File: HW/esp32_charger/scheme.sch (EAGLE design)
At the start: 23 parts, among them IC3 24C01SN, K1 4052, T1 2N7002E, T2 2N7002E

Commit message: Updated project and gitignore
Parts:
- added C2: 10uF, rcl:C-EUC0805
- added C2-TANT: 22uF, rcl:C-EUC3216
- added IC1: LM1117IMPX-3.3, lm1117:LM1117IMPX-3.3
- added LED1: (no value), led:LEDCHIP-LED0805
- added R9: 500, rcl:R-EU_R0805
- added SV2: (no value), con-lstb:MA03-1
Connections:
- new net +3V3: C2-TANT.1, IC1.OUT, IC1.OUT1, U$1.3V3
- new net +5V: C2.1, IC1.IN, R9.2, SV2.2
- new net N$1: LED1.A, R9.1
- net GND: now also C2-TANT.2, C2.2, IC1.GND, LED1.C, SV2.1
- net VCC: no longer U$1.3V3
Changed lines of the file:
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@@
 <?xml version="1.0" encoding="utf-8"?>
 <!DOCTYPE eagle SYSTEM "eagle.dtd">
-<eagle version="9.3.2">
+<eagle version="9.4.2">
 <drawing>
 <settings>
@@
 <setting verticaltext="up"/>
 </settings>
-<grid distance="0.1" unitdist="inch" unit="inch" style="dots" multiple="1" display="yes" altdistance="0.01" altunitdist="inch" altunit="inch"/>
+<grid distance="0.1" unitdist="inch" unit="inch" style="lines" multiple="1" display="no" altdistance="0.01" altunitdist="inch" altunit="inch"/>
 <layers>
 <layer number="1" name="Top" color="4" fill="1" visible="no" active="no"/>
@@
 <layer number="230" name="230bmp" color="7" fill="1" visible="yes" active="yes"/>
 <layer number="231" name="231bmp" color="7" fill="1" visible="yes" active="yes"/>
+<layer number="232" name="Eagle3D_PG2" color="7" fill="1" visible="no" active="no"/>
+<layer number="233" name="Eagle3D_PG3" color="7" fill="1" visible="no" active="no"/>
 <layer number="248" name="Housing" color="7" fill="1" visible="yes" active="yes"/>
 <layer number="249" name="Edge" color="7" fill="1" visible="yes" active="yes"/>
@@
 <part name="K1" library="relay" library_urn="urn:adsk.eagle:library:339" deviceset="4052" device="" package3d_urn="urn:adsk.eagle:package:24305/1"/>
 <part name="T1" library="nxp_60" deviceset="2N7002" device="" technology="E"/>
-<part name="SUPPLY1" library="SparkFun-PowerSymbols" library_urn="urn:adsk.eagle:library:530" deviceset="VCC" device=""/>
 <part name="GND1" library="SparkFun-PowerSymbols" library_urn="urn:adsk.eagle:library:530" deviceset="GND" device=""/>
 <part name="SUPPLY2" library="SparkFun-PowerSymbols" library_urn="urn:adsk.eagle:library:530" deviceset="VCC" device=""/>
@@
 <part name="R8" library="antduino" deviceset="SPARKFUN_RESISTOR" device="PTH-1/2W" value="10K"/>
 <part name="SUPPLY4" library="SparkFun-PowerSymbols" library_urn="urn:adsk.eagle:library:530" deviceset="VCC" device=""/>
+<part name="IC1" library="lm1117" deviceset="LM1117IMPX-*" device="" technology="3.3"/>
+<part name="GND8" library="supply1" library_urn="urn:adsk.eagle:library:371" deviceset="GND" device=""/>
+<part name="P+1" library="supply1" library_urn="urn:adsk.eagle:library:371" deviceset="+5V" device=""/>
+<part name="SV2" library="con-lstb" library_urn="urn:adsk.eagle:library:162" deviceset="MA03-1" device="" package3d_urn="urn:adsk.eagle:package:8339/1"/>
+<part name="+3V1" library="supply1" library_urn="urn:adsk.eagle:library:371" deviceset="+3V3" device=""/>
+<part name="+3V2" library="supply1" library_urn="urn:adsk.eagle:library:371" deviceset="+3V3" device=""/>
+<part name="C2" library="rcl" library_urn="urn:adsk.eagle:library:334" deviceset="C-EU" device="C0805" package3d_urn="urn:adsk.eagle:package:23617/2" value="10uF"/>
+<part name="C2-TANT" library="rcl" library_urn="urn:adsk.eagle:library:334" deviceset="C-EU" device="C3216" package3d_urn="urn:adsk.eagle:package:23628/2" value="22uF"/>
+<part name="R9" library="rcl" library_urn="urn:adsk.eagle:library:334" deviceset="R-EU_" device="R0805" package3d_urn="urn:adsk.eagle:package:23553/2" value="500"/>
+<part name="LED1" library="led" library_urn="urn:adsk.eagle:library:259" deviceset="LED" device="CHIP-LED0805" package3d_urn="urn:adsk.eagle:package:15818/2"/>
 </parts>
 <sheets>
@@
 <attribute name="NAME" x="-2.54" y="90.17" size="1.778" layer="95" font="vector" rot="R180"/>
 </instance>
-<instance part="SUPPLY1" gate="G$1" x="55.88" y="45.72" smashed="yes" rot="R180">
-<attribute name="VALUE" x="55.88" y="42.926" size="1.778" layer="96" rot="R270" align="bottom-center"/>
-</instance>
 <instance part="GND1" gate="1" x="60.96" y="38.1" smashed="yes">
 <attribute name="VALUE" x="60.96" y="37.846" size="1.778" layer="96" align="top-center"/>
@@
 <instance part="SUPPLY4" gate="G$1" x="114.3" y="0" smashed="yes">
 <attribute name="VALUE" x="114.3" y="2.794" size="1.778" layer="96" rot="R90" align="bottom-center"/>
+</instance>
+<instance part="IC1" gate="G$1" x="30.48" y="2.54" smashed="yes">
+<attribute name="NAME" x="33.02" y="-5.08" size="1.778" layer="95"/>
+<attribute name="VALUE" x="20.32" y="10.16" size="1.778" layer="96"/>
+</instance>
+<instance part="GND8" gate="1" x="30.48" y="-30.48" smashed="yes">
+<attribute name="VALUE" x="27.94" y="-33.02" size="1.778" layer="96"/>
+</instance>
+<instance part="P+1" gate="1" x="-5.08" y="5.08" smashed="yes">
+<attribute name="VALUE" x="-7.62" y="0" size="1.778" layer="96" rot="R90"/>
+</instance>
+<instance part="SV2" gate="G$1" x="-5.08" y="-33.02" smashed="yes" rot="R90">
+<attribute name="VALUE" x="2.54" y="-34.29" size="1.778" layer="96" rot="R90"/>
+<attribute name="NAME" x="-10.922" y="-34.29" size="1.778" layer="95" rot="R90"/>
+</instance>
+<instance part="+3V1" gate="G$1" x="66.04" y="55.88" smashed="yes">
+<attribute name="VALUE" x="63.5" y="50.8" size="1.778" layer="96" rot="R90"/>
+</instance>
+<instance part="+3V2" gate="G$1" x="58.42" y="10.16" smashed="yes">
+<attribute name="VALUE" x="55.88" y="5.08" size="1.778" layer="96" rot="R90"/>
+</instance>
+<instance part="C2" gate="G$1" x="15.24" y="0" smashed="yes">
+<attribute name="NAME" x="16.764" y="0.381" size="1.778" layer="95"/>
+<attribute name="VALUE" x="16.764" y="-4.699" size="1.778" layer="96"/>
+</instance>
+<instance part="C2-TANT" gate="G$1" x="45.72" y="2.54" smashed="yes">
+<attribute name="NAME" x="47.244" y="2.921" size="1.778" layer="95"/>
+<attribute name="VALUE" x="47.244" y="-2.159" size="1.778" layer="96"/>
+</instance>
+<instance part="R9" gate="G$1" x="2.54" y="-2.54" smashed="yes" rot="R90">
+<attribute name="NAME" x="1.0414" y="-6.35" size="1.778" layer="95" rot="R90"/>
+<attribute name="VALUE" x="5.842" y="-6.35" size="1.778" layer="96" rot="R90"/>
+</instance>
+<instance part="LED1" gate="G$1" x="2.54" y="-12.7" smashed="yes">
+<attribute name="NAME" x="6.096" y="-17.272" size="1.778" layer="95" rot="R90"/>
+<attribute name="VALUE" x="8.255" y="-17.272" size="1.778" layer="96" rot="R90"/>
 </instance>
 </instances>
@@
 <nets>
 <net name="VCC" class="0">
-<segment>
-<pinref part="U$1" gate="G$1" pin="3V3"/>
-<pinref part="SUPPLY1" gate="G$1" pin="VCC"/>
-<wire x1="55.88" y1="48.26" x2="55.88" y2="45.72" width="0.1524" layer="91"/>
-</segment>
 <segment>
 <pinref part="U$3" gate="G$1" pin="VCC"/>
@@
 <wire x1="114.3" y1="-29.464" x2="114.3" y2="-27.94" width="0.1524" layer="91"/>
 <junction x="114.3" y="-27.94"/>
+</segment>
+<segment>
+<pinref part="IC1" gate="G$1" pin="GND"/>
+<pinref part="SV2" gate="G$1" pin="1"/>
+<wire x1="-2.54" y1="-25.4" x2="2.54" y2="-25.4" width="0.1524" layer="91"/>
+<wire x1="2.54" y1="-25.4" x2="30.48" y2="-25.4" width="0.1524" layer="91"/>
+<wire x1="30.48" y1="-25.4" x2="30.48" y2="-5.08" width="0.1524" layer="91"/>
+<pinref part="GND8" gate="1" pin="GND"/>
+<wire x1="30.48" y1="-27.94" x2="30.48" y2="-25.4" width="0.1524" layer="91"/>
+<junction x="30.48" y="-25.4"/>
+<pinref part="LED1" gate="G$1" pin="C"/>
+<wire x1="2.54" y1="-17.78" x2="2.54" y2="-25.4" width="0.1524" layer="91"/>
+<junction x="2.54" y="-25.4"/>
+<pinref part="C2" gate="G$1" pin="2"/>
+<wire x1="15.24" y1="-5.08" x2="30.48" y2="-5.08" width="0.1524" layer="91"/>
+<junction x="30.48" y="-5.08"/>
+<pinref part="C2-TANT" gate="G$1" pin="2"/>
+<wire x1="45.72" y1="-2.54" x2="45.72" y2="-5.08" width="0.1524" layer="91"/>
+<wire x1="45.72" y1="-5.08" x2="30.48" y2="-5.08" width="0.1524" layer="91"/>
 </segment>
 </net>
@@
 </segment>
 </net>
+<net name="+5V" class="0">
+<segment>
+<pinref part="P+1" gate="1" pin="+5V"/>
+<pinref part="IC1" gate="G$1" pin="IN"/>
+<wire x1="-5.08" y1="2.54" x2="2.54" y2="2.54" width="0.1524" layer="91"/>
+<pinref part="SV2" gate="G$1" pin="2"/>
+<wire x1="2.54" y1="2.54" x2="15.24" y2="2.54" width="0.1524" layer="91"/>
+<wire x1="15.24" y1="2.54" x2="22.86" y2="2.54" width="0.1524" layer="91"/>
+<wire x1="-5.08" y1="-25.4" x2="-5.08" y2="2.54" width="0.1524" layer="91"/>
+<junction x="-5.08" y="2.54"/>
+<pinref part="R9" gate="G$1" pin="2"/>
+<junction x="2.54" y="2.54"/>
+<pinref part="C2" gate="G$1" pin="1"/>
+<junction x="15.24" y="2.54"/>
+</segment>
+</net>
+<net name="+3V3" class="0">
+<segment>
+<pinref part="IC1" gate="G$1" pin="OUT"/>
+<pinref part="IC1" gate="G$1" pin="OUT1"/>
+<wire x1="38.1" y1="2.54" x2="38.1" y2="5.08" width="0.1524" layer="91"/>
+<pinref part="+3V2" gate="G$1" pin="+3V3"/>
+<wire x1="38.1" y1="5.08" x2="45.72" y2="5.08" width="0.1524" layer="91"/>
+<wire x1="45.72" y1="5.08" x2="58.42" y2="5.08" width="0.1524" layer="91"/>
+<wire x1="58.42" y1="5.08" x2="58.42" y2="7.62" width="0.1524" layer="91"/>
+<junction x="38.1" y="5.08"/>
+<pinref part="C2-TANT" gate="G$1" pin="1"/>
+<junction x="45.72" y="5.08"/>
+</segment>
+<segment>
+<pinref part="U$1" gate="G$1" pin="3V3"/>
+<wire x1="55.88" y1="48.26" x2="66.04" y2="48.26" width="0.1524" layer="91"/>
+<pinref part="+3V1" gate="G$1" pin="+3V3"/>
+<wire x1="66.04" y1="48.26" x2="66.04" y2="53.34" width="0.1524" layer="91"/>
+</segment>
+</net>
+<net name="N$1" class="0">
+<segment>
+<pinref part="R9" gate="G$1" pin="1"/>
+<pinref part="LED1" gate="G$1" pin="A"/>
+<wire x1="2.54" y1="-10.16" x2="2.54" y2="-7.62" width="0.1524" layer="91"/>
+</segment>
+</net>

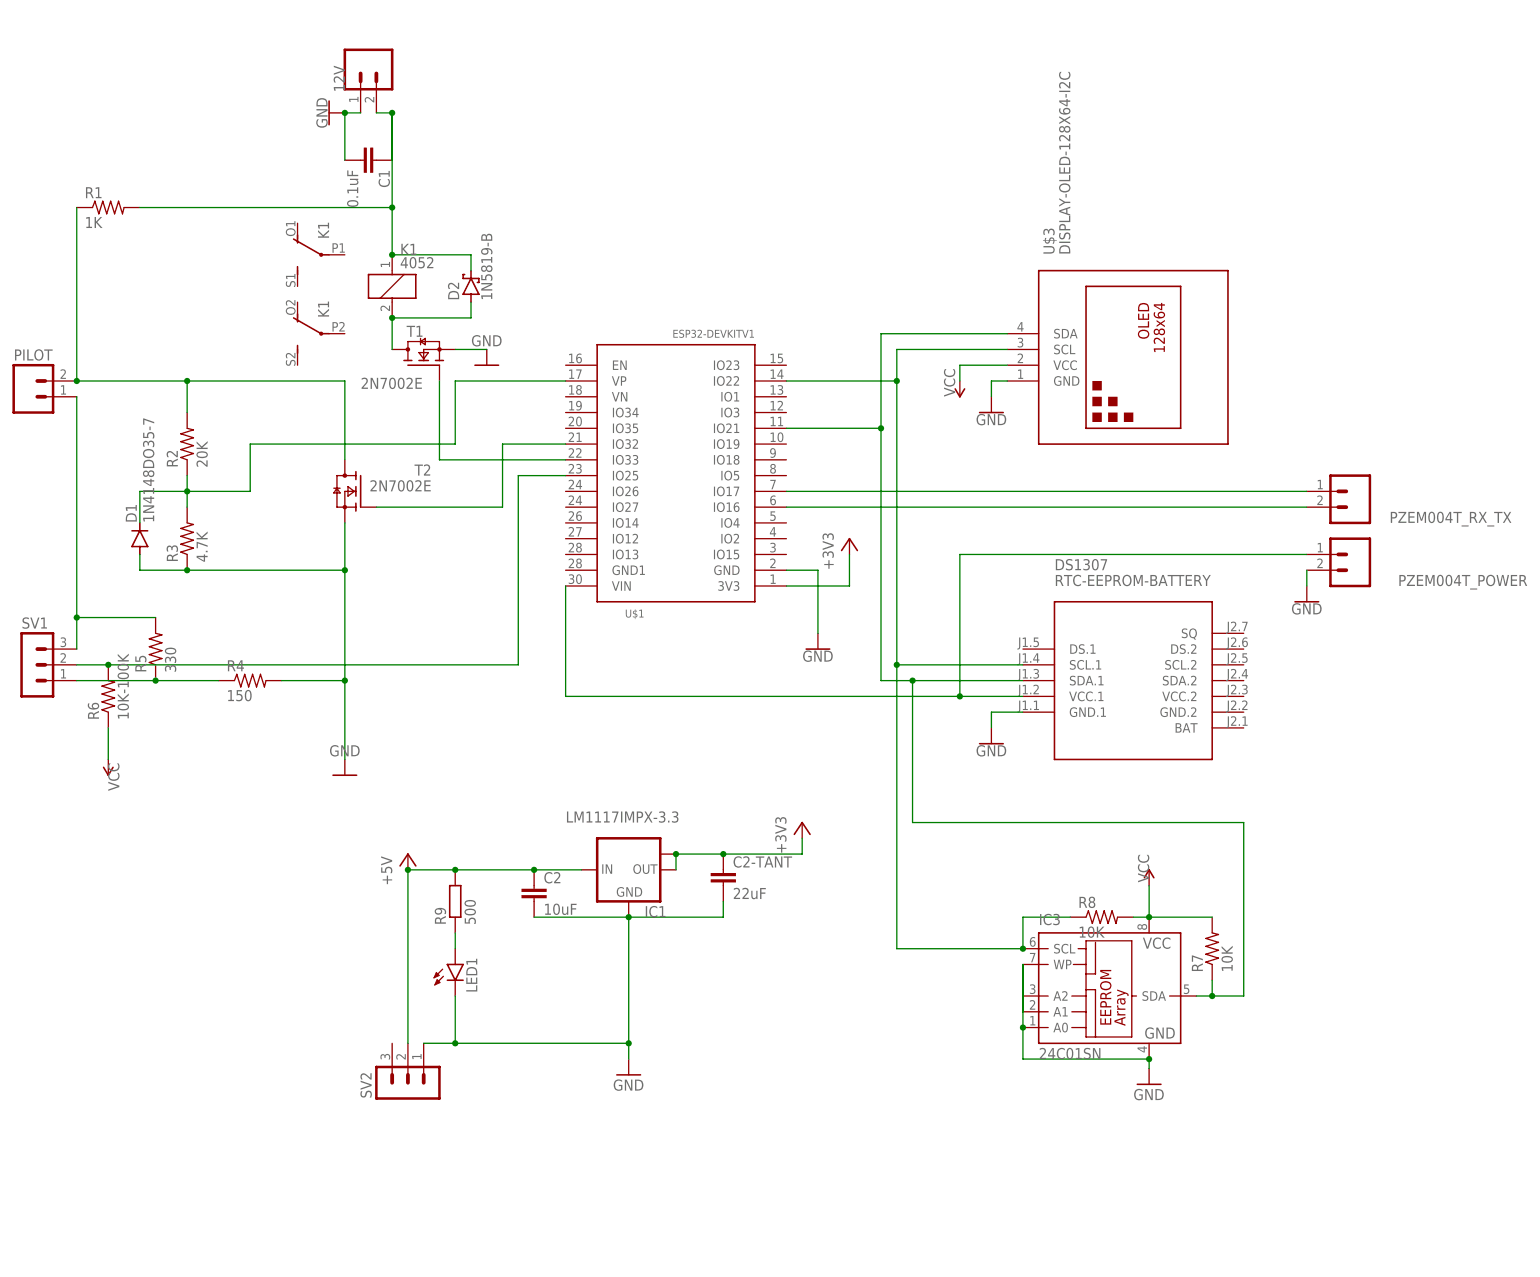
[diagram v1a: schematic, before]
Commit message: Added bare esp32 and ds1307
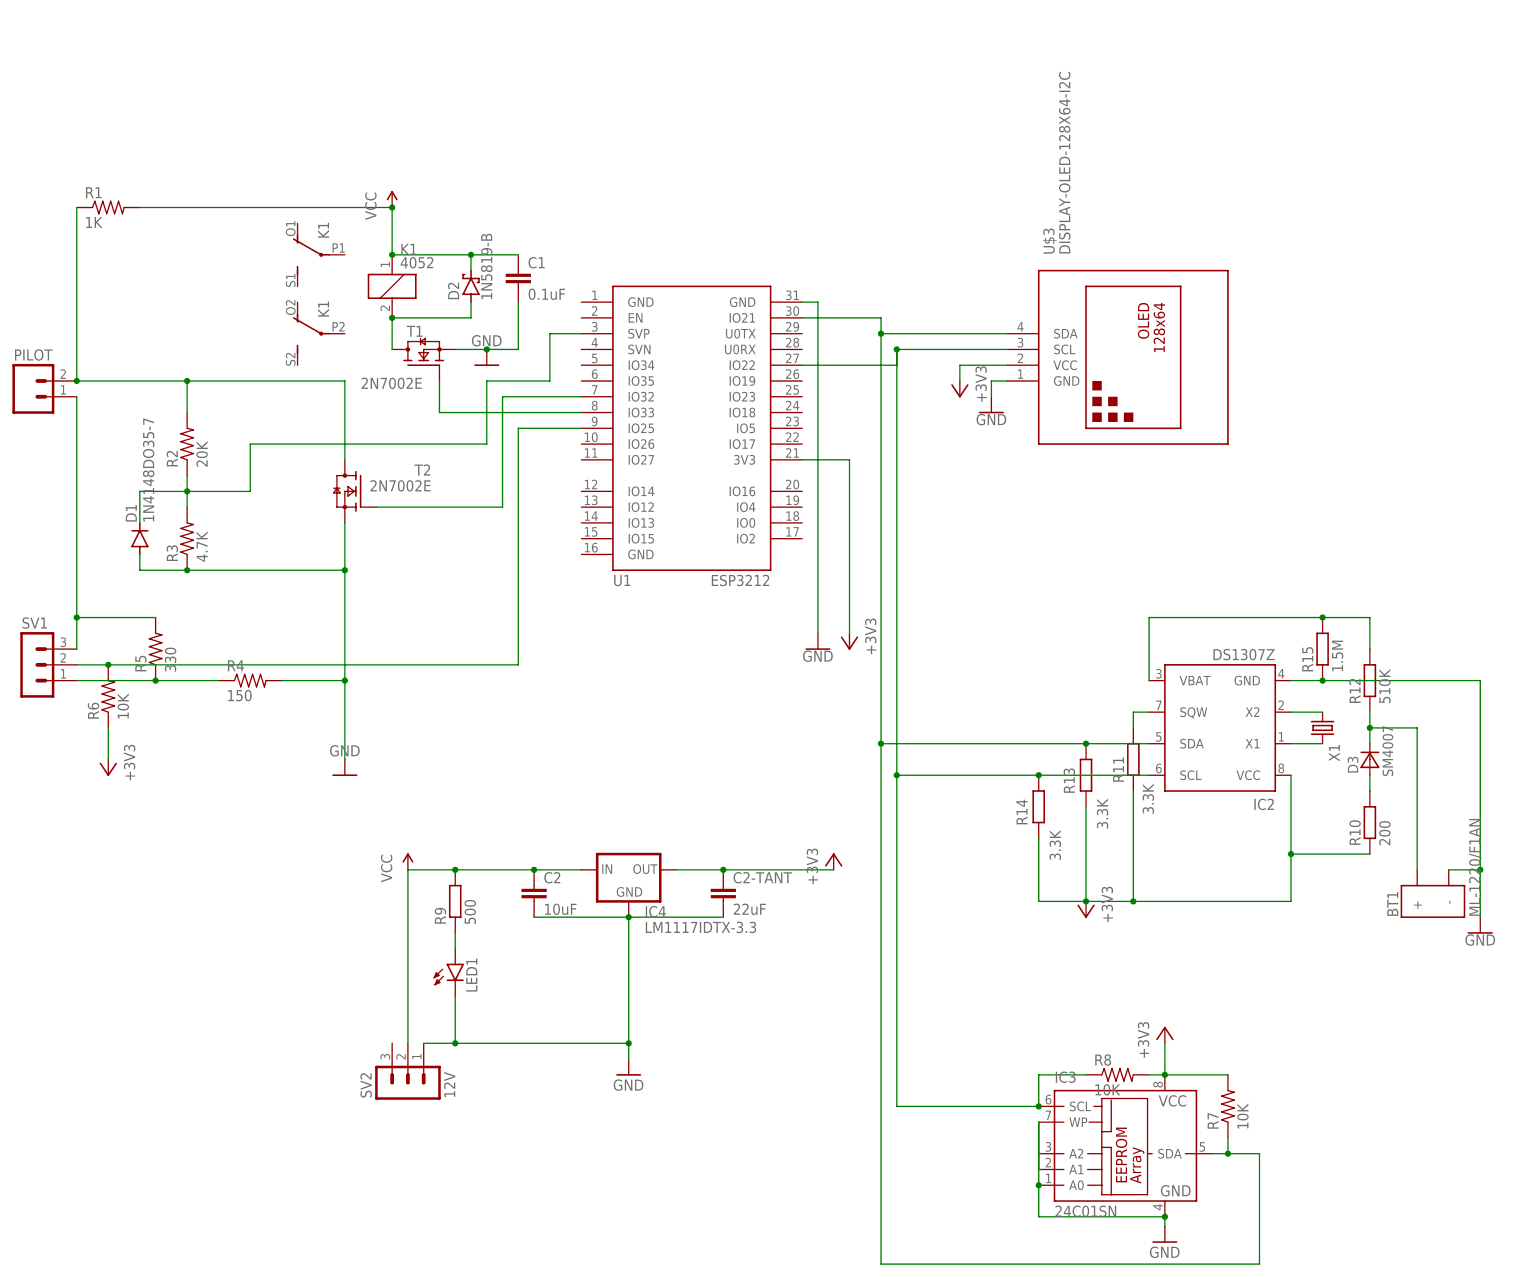
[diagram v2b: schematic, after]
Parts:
- removed 12V, PZEM004T_POWER, PZEM004T_RX_TX: (no value), antduino:SPARKFUN_M02PTH
- removed DS1307: RTC-EEPROM-BATTERY, diy-modules:RTC-EEPROM-BATTERY
- removed IC1: LM1117IMPX-3.3, lm1117:LM1117IMPX-3.3
- removed U$1: ESP32DEVKITV1, ESP32-DEVKITV1:ESP32DEVKITV1
- added BT1: ML-1220/F1AN, batteries:ML-1220/F1AN
- added D3: SM4007, _mod_diode:SM4007
- added IC2: DS1307Z, ds1307_pcf8583:DS1307Z
- added IC4: LM1117IDTX-3.3, lm1117:LM1117IDTX-3.3
- added R10: 200, rcl:R-EU_R0805
- added R11, R13, R14: 3.3K, rcl:R-EU_R0805
- added R12: 510K, rcl:R-EU_R0805
- added R15: 1.5M, rcl:R-EU_R0805
- added U1: ESP3212, esp32:ESP3212
- added X1: CRYSTALS-NOGND-WATCH-3X8, IQD-Frequency-Products:CRYSTALS-NOGND-WATCH-3X8
- R6: value 10K-100K -> 10K
- SV2: value (none) -> 12V
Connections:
- removed net +5V: C2.1, IC1.IN, R9.2, SV2.2
- removed net N$3: DS1307.VCC.1, PZEM004T_POWER.1, U$1.VIN
- removed net N$4: PZEM004T_RX_TX.1, U$1.IO17
- removed net N$5: PZEM004T_RX_TX.2, U$1.IO16
- removed net N$7: 12V.2, C1.1, D2.C, K11.1, R1.2
- new net N$16: IC2.X2, X1.1
- new net N$17: IC2.SCL, IC3.SCL, R14.1, R8.1, U$3.SCL, U1.IO22
- new net N$18: IC2.SDA, IC3.SDA, R13.1, R7.1, U$3.SDA, U1.IO21
- new net N$19: IC2.VBAT, R12.2, R15.2
- new net N$2: IC2.X1, X1.2
- new net N$20: BT1.+, D3.C, R12.1
- net +3V3: now also IC2.VCC, IC3.VCC, IC4.OUT, R10.1, R11.1, R13.2, R14.2, R6.1, R7.2, R8.2, U$3.VCC, U1.3V3; no longer IC1.OUT, IC1.OUT1, U$1.3V3
- net GND: now also BT1.-, IC2.GND, IC4.GND, R15.1, U1.GND@3; no longer 12V.1, DS1307.GND.1, IC1.GND, PZEM004T_POWER.2, U$1.GND
- net N$11: now also U1.SVP; no longer U$1.VP
- net N$14: now also U1.IO25; no longer U$1.IO25
- net N$15: now also IC2.SQW, R11.2; no longer DS1307.SCL.1, IC3.SCL, R8.1, U$1.IO22, U$3.SCL
- net N$22: now also D3.A, R10.2; no longer DS1307.SDA.1, IC3.SDA, R7.1, U$1.IO21, U$3.SDA
- net N$6: now also U1.IO33; no longer U$1.IO33
- net N$9: now also U1.IO32; no longer U$1.IO32
- net VCC: now also C1.1, C2.1, D2.C, IC4.IN, K11.1, R1.2, R9.2, SV2.2; no longer IC3.VCC, R6.1, R7.2, R8.2, U$3.VCC
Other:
- moved on the sheet: C1, C2-TANT, IC3, R7, R8
